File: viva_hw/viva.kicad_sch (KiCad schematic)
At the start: 41 parts, among them J1 Motor, J2 EMG, J3 Battery, J4 OLED, J5 Battery, M1 XIAO_ESP32C3, Q1 NMOS, Q2 NMOS, Q3 NMOS, Q4 NMOS, SW1 SW_DPDT_x2, SW2 SW_DPST_x2, SW3 SW_DPST_x2, U1 LM358, U2 LM358

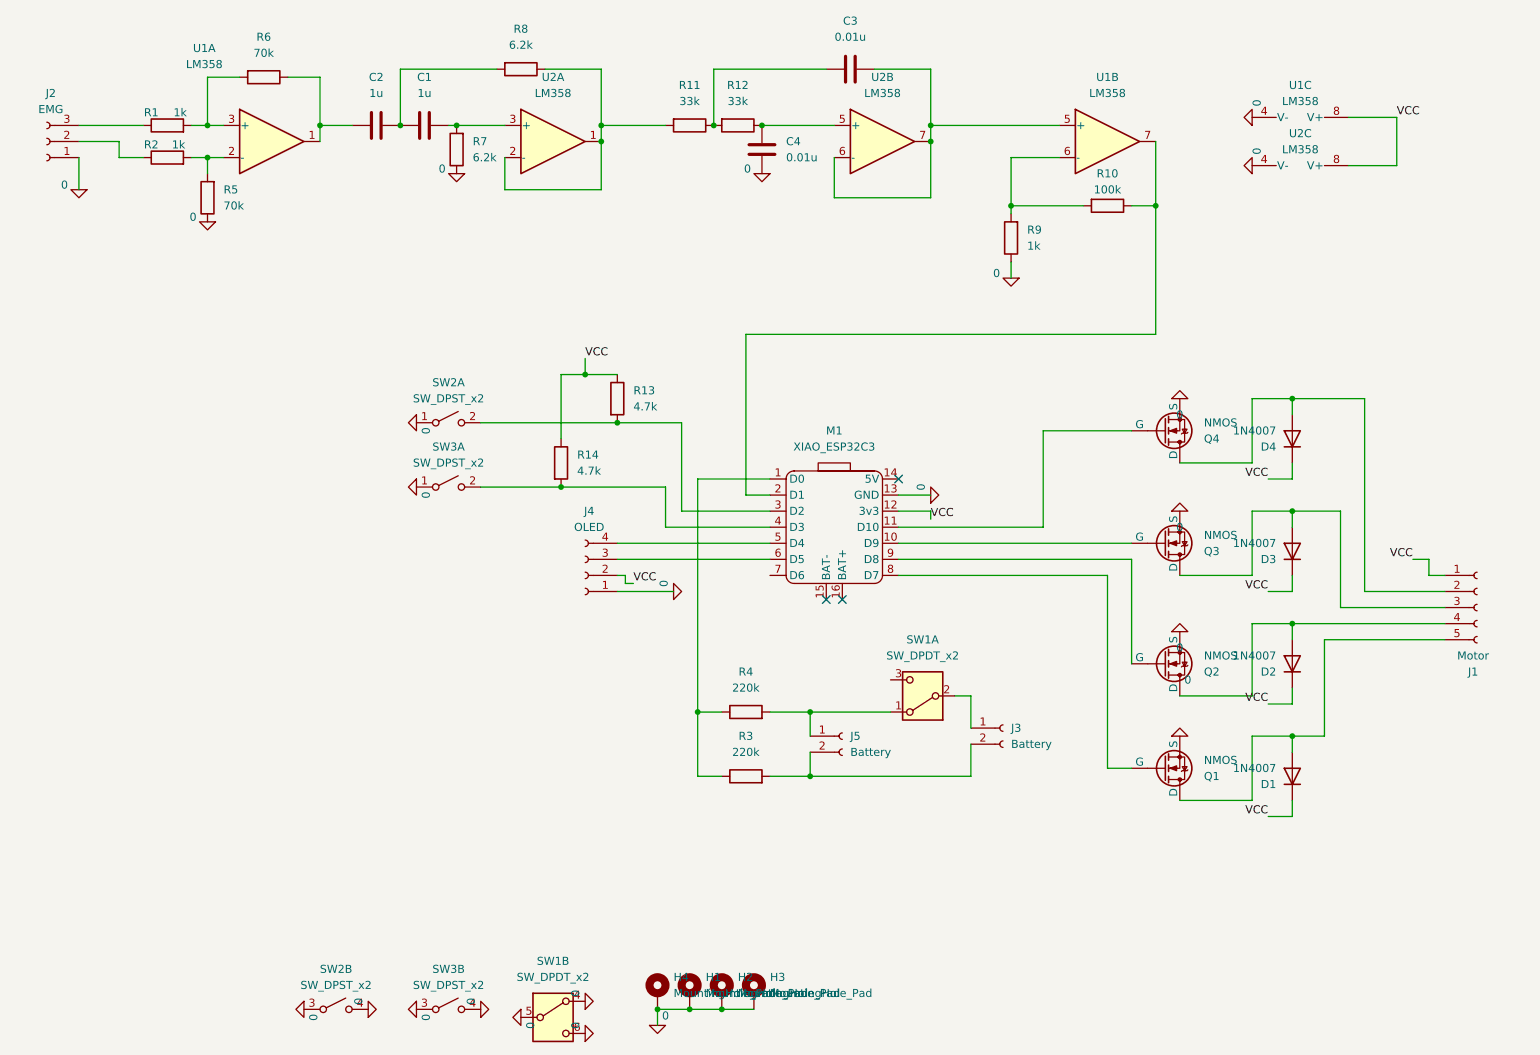
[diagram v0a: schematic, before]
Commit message: feat: removed analog
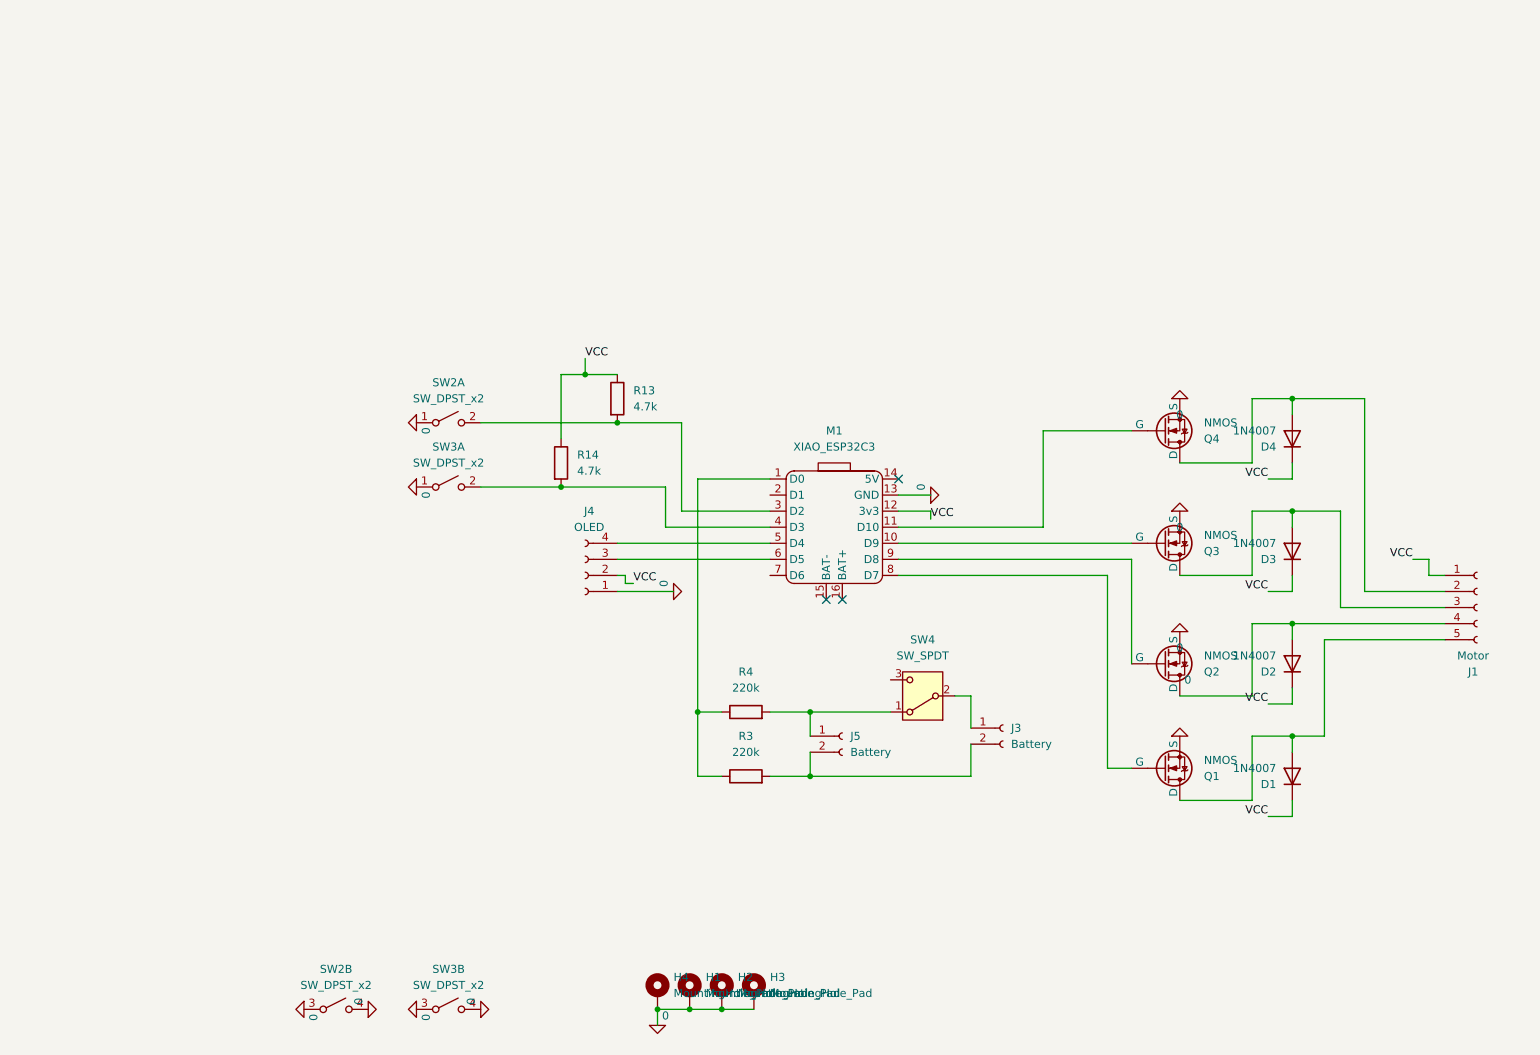
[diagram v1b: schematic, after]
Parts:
- removed C1, C2: 1u, symbol Device:C
- removed C3, C4: 0.01u, symbol Device:C
- removed J2: EMG, Connector_PinHeader_2.54mm:PinHeader_1x03_P2.54mm_Vertical, symbol Connector:Conn_01x03_Socket
- removed R1, R2, R9: 1k, symbol Device:R
- removed R10: 100k, symbol Device:R
- removed R11, R12: 33k, symbol Device:R
- removed R5, R6: 70k, symbol Device:R
- removed R7, R8: 6.2k, symbol Device:R
- removed SW1: SW_DPDT_x2, symbol Switch:SW_DPDT_x2
- removed U1, U2: LM358, Package_DIP:DIP-8_W7.62mm_Socket, symbol Amplifier_Operational:LM358
- added SW4: SW_SPDT, Additional_Switches:SPDT, symbol Switch:SW_SPDT
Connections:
- net at J3.1 (Pin_1): now also SW4.2 (B)
- net at J5.1 (Pin_1), R4.2: now also SW4.1 (A)

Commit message: feat: dont remember
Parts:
- J4: footprint (none) -> Connector_PinHeader_2.54mm:PinHeader_1x04_P2.54mm_Vertical
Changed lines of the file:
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@@
 			)
 		)
-		(property "Footprint" ""
+		(property "Footprint" "Connector_PinHeader_2.54mm:PinHeader_1x04_P2.54mm_Vertical"
 			(at 107.95 106.68 0)
 			(effects

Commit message: feat: finished schematic
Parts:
- removed SW4: SW_SPDT, Additional_Switches:SPDT, symbol Switch:SW_SPDT
- added C1, C2, C3, C4: 100n, Capacitor_THT:C_Disc_D4.3mm_W1.9mm_P5.00mm, symbol Device:C
- added C5, C6: 100u, Capacitor_THT:CP_Radial_D8.0mm_P3.50mm, symbol Device:C
- added J2: Measure_enable, Connector_PinHeader_2.54mm:PinHeader_1x02_P2.54mm_Vertical, symbol Connector:Conn_01x02_Socket
- added SW1: SW_DPDT_x2, Additional_Switches:SK-22D07G4, symbol Switch:SW_DPDT_x2
- D1, D2, D3, D4: value 1N4007 -> 1N4148; footprint Diode_THT:D_DO-41_SOD81_P10.16mm_Horizontal -> Diode_THT:D_DO-34_SOD68_P7.62mm_Horizontal
- H1, H2, H3, H4: footprint MountingHole:MountingHole_2.7mm_M2.5_DIN965_Pad -> MountingHole:MountingHole_3.2mm_M3_ISO7380_Pad
- J3: value Battery -> Battery_in; footprint Connector_PinHeader_2.54mm:PinHeader_1x02_P2.54mm_Vertical -> Connector_PinHeader_2.00mm:PinHeader_1x02_P2.00mm_Vertical
- J4: footprint Connector_PinHeader_2.54mm:PinHeader_1x04_P2.54mm_Vertical -> Additional_Display:OLED_0.96
- J5: value Battery -> Battery_out; footprint Connector_PinHeader_2.54mm:PinHeader_1x02_P2.54mm_Vertical -> Connector_PinHeader_2.00mm:PinHeader_1x02_P2.00mm_Vertical
- Q1, Q2, Q3, Q4: footprint Package_TO_SOT_THT:TO-126-3_Vertical -> Package_TO_SOT_THT:TO-92L_Inline
- R13, R14: value 4.7k -> 5.6k; footprint (none) -> Resistor_THT:R_Axial_DIN0207_L6.3mm_D2.5mm_P10.16mm_Horizontal
- R3, R4: footprint (none) -> Resistor_THT:R_Axial_DIN0207_L6.3mm_D2.5mm_P10.16mm_Horizontal
- SW2, SW3: footprint (none) -> Additional_Switches:TACTILE-2P-THT
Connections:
- net 0: now also J3.1 (Pin_1), J5.1 (Pin_1), C5.2, C6.2, J2.2 (Pin_2); no longer SW2.3 (A), SW2.4 (B), SW3.3 (A), SW3.4 (B)
- net VCC: now also J5.2 (Pin_2), R3.2, C1.1, C2.1, C3.1, C4.1, C5.1, C6.1, SW1.3 (C); no longer J4.2 (Pin_2), M1.12 (3v3)
- net at D4.2 (A), J1.2 (Pin_2), Q4.1 (D): now also C4.2
- net at D3.2 (A), J1.3 (Pin_3), Q3.1 (D): now also C3.2
- net at D2.2 (A), J1.4 (Pin_4), Q2.1 (D): now also C2.2
- net at D1.2 (A), J1.5 (Pin_5), Q1.1 (D): now also C1.2
- net at R4.2: now also J2.1 (Pin_1); no longer J5.1 (Pin_1)
- new net: J3.2 (Pin_2), SW1.2 (B)
- new net: J4.2 (Pin_2), M1.12 (3v3)
- no-connect marks 3 -> 13
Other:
- moved on the sheet: D1, D2, D3, D4, H1, H2, H3, H4, J1, J3, J4, J5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

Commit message: feat: completed v_1
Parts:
- added R1, R2, R5, R6: 100, Resistor_THT:R_Axial_DIN0207_L6.3mm_D2.5mm_P10.16mm_Horizontal, symbol Device:R
- R3, R4: value 220k -> 5.6k
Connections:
- net at M1.11 (D10): now also R1.1; no longer Q4.2 (G)
- net at Q3.2 (G): now also R2.2; no longer M1.10 (D9)
- net at M1.8 (D7): now also R6.1; no longer Q1.2 (G)
- net at M1.9 (D8): now also R5.1; no longer Q2.2 (G)
- new net: Q1.2 (G), R6.2
- new net: Q4.2 (G), R1.2
- new net: M1.10 (D9), R2.1
- new net: Q2.2 (G), R5.2

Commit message: feat: v2, changed controller
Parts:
- removed C5: 100u, Capacitor_THT:CP_Radial_D8.0mm_P3.50mm, symbol Device:C
- removed J2: Measure_enable, Connector_PinHeader_2.54mm:PinHeader_1x02_P2.54mm_Vertical, symbol Connector:Conn_01x02_Socket
- removed J5: Battery_out, Connector_PinHeader_2.00mm:PinHeader_1x02_P2.00mm_Vertical, symbol Connector:Conn_01x02_Socket
- removed M1: XIAO_ESP32C3, System_On_Chip:XIAO_ESP32C3_THR, symbol System_On_Chip:XIAO_ESP32C3
- removed R3, R4: 5.6k, Resistor_THT:R_Axial_DIN0207_L6.3mm_D2.5mm_P10.16mm_Horizontal, symbol Device:R
- added M2: ESP32C3_Super_Mini, System_On_Chip:ESP32C3_SUPER_MINI_THR, symbol System_On_Chip:ESP32C3_Super_Mini
- J3: value Battery_in -> Power_in; footprint Connector_PinHeader_2.00mm:PinHeader_1x02_P2.00mm_Vertical -> Additional_Connectors:Barrel_Plug_5.5mmx2.1mm
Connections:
- net VCC is gone; now on net +3V3: C1.1, C2.1, C3.1, C4.1, C6.1, D1.1 (K), D2.1 (K), D3.1 (K), D4.1 (K), J1.1 (Pin_1), R13.1, R14.1, SW1.3 (C)
- net 0: now also Q1.1 (D), Q2.1 (D), Q3.1 (D), Q4.1 (D), M2.15 (GND); no longer Q1.3 (S), Q2.3 (S), Q3.3 (S), Q4.3 (S)
- net at C4.2, D4.2 (A), J1.2 (Pin_2): now also Q4.3 (S); no longer Q4.1 (D)
- net at C2.2, D2.2 (A), J1.4 (Pin_4): now also Q2.3 (S); no longer Q2.1 (D)
- net at R14.2, SW3.2 (B): now also M2.13 (D2)
- net at R6.1: now also M2.1 (D3)
- net at C3.2, D3.2 (A), J1.3 (Pin_3): now also Q3.3 (S); no longer Q3.1 (D)
- net at C1.2, D1.2 (A), J1.5 (Pin_5): now also Q1.3 (S); no longer Q1.1 (D)
- net at R1.1: now also M2.8 (D6)
- net +3V3: now reaches J4.2 (Pin_2)
- net +3V3: now also M2.14 (3v3)
- net at J4.3 (Pin_3): now also M2.3 (D5)
- net at J4.4 (Pin_4): now also M2.2 (D4)
- net at R13.2, SW2.2 (B): now also M2.12 (D1)
- net at R2.1: now also M2.7 (D7)
- net at R5.1: now also M2.6 (D10)
- no-connect marks 13 -> 14
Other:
- moved on the sheet: C1, C2, C3, C4, C6, D1, D2, D3, D4, J1, J3, J4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
